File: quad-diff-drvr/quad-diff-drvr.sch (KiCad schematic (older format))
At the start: 58 parts, among them J1 Raspberry_Pi_2_3, J2 Conn_01x04, J3 Conn_01x04, J4 Conn_01x04, J5 Conn_01x04, J6 Conn_01x04, U1 INA3221, U2 74LS153, U3 74LS153, U4 74LS153, U5 PCA9555PW, U6 LTC1688, U7 SLG5NT1581V, U8 SLG5NT1581V

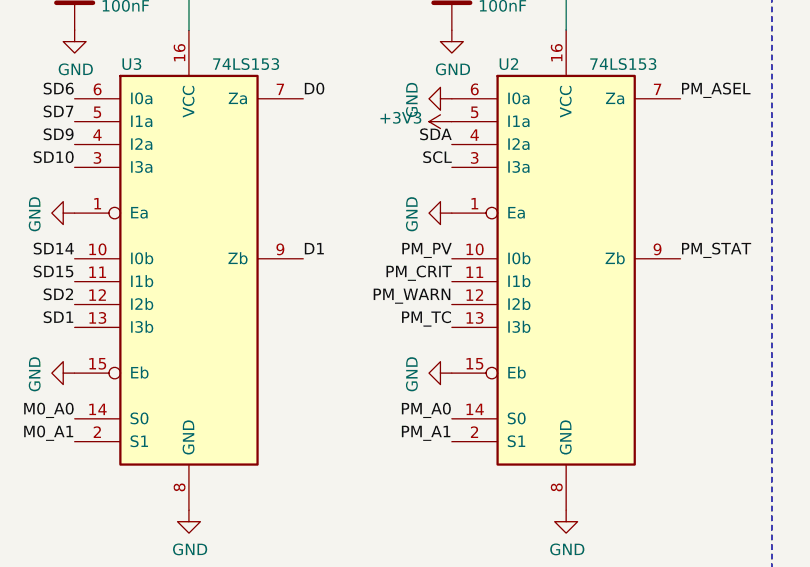
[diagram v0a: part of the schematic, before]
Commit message: qdd: two high-side switches in
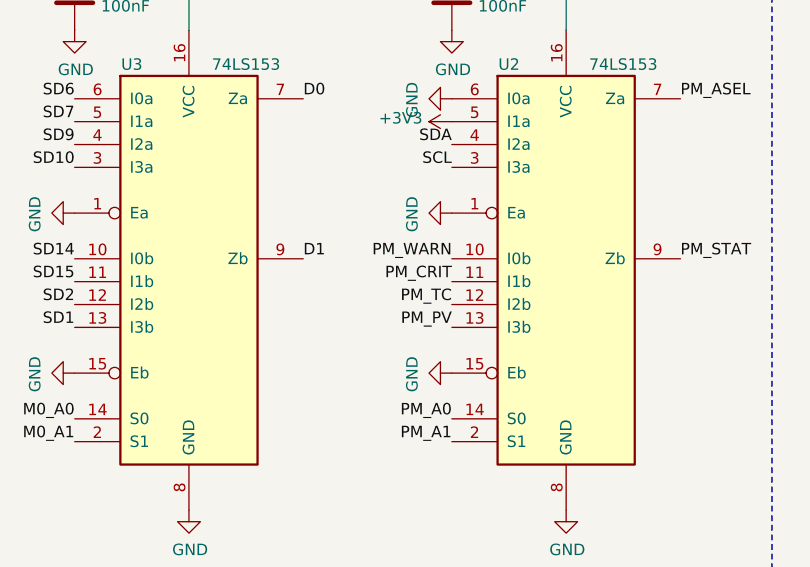
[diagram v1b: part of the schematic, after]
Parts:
- C14, C17: footprint Capacitor_SMD:C_0603_1608Metric -> Capacitor_SMD:C_1206_3216Metric
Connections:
- net PM_PV: now also U2.13 (I3b); no longer U2.10 (I0b)
- net PM_TC: now also U2.12 (I2b); no longer U2.13 (I3b)
- net PM_WARN: now also U2.10 (I0b); no longer U2.12 (I2b)
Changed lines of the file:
@@
 Text Label 5900 6000 2    50   ~ 0
 SCL
-Text Label 5900 6400 2    50   ~ 0
+Text Label 5900 6700 2    50   ~ 0
 PM_PV
 Text Label 5900 6500 2    50   ~ 0
 PM_CRIT
+Text Label 5900 6400 2    50   ~ 0
+PM_WARN
 Text Label 5900 6600 2    50   ~ 0
-PM_WARN
-Text Label 5900 6700 2    50   ~ 0
 PM_TC
 $Comp
@@
 F 0 "C14" H 8615 1246 50  0000 L CNN
 F 1 "10uF" H 8615 1155 50  0000 L CNN
-F 2 "Capacitor_SMD:C_0603_1608Metric" H 8538 1050 50  0001 C CNN
+F 2 "Capacitor_SMD:C_1206_3216Metric" H 8538 1050 50  0001 C CNN
 F 3 "~" H 8500 1200 50  0001 C CNN
 	1    8500 1200
@@
 F 0 "C17" H 10415 1246 50  0000 L CNN
 F 1 "10uF" H 10415 1155 50  0000 L CNN
-F 2 "Capacitor_SMD:C_0603_1608Metric" H 10338 1050 50  0001 C CNN
+F 2 "Capacitor_SMD:C_1206_3216Metric" H 10338 1050 50  0001 C CNN
 F 3 "~" H 10300 1200 50  0001 C CNN
 	1    10300 1200

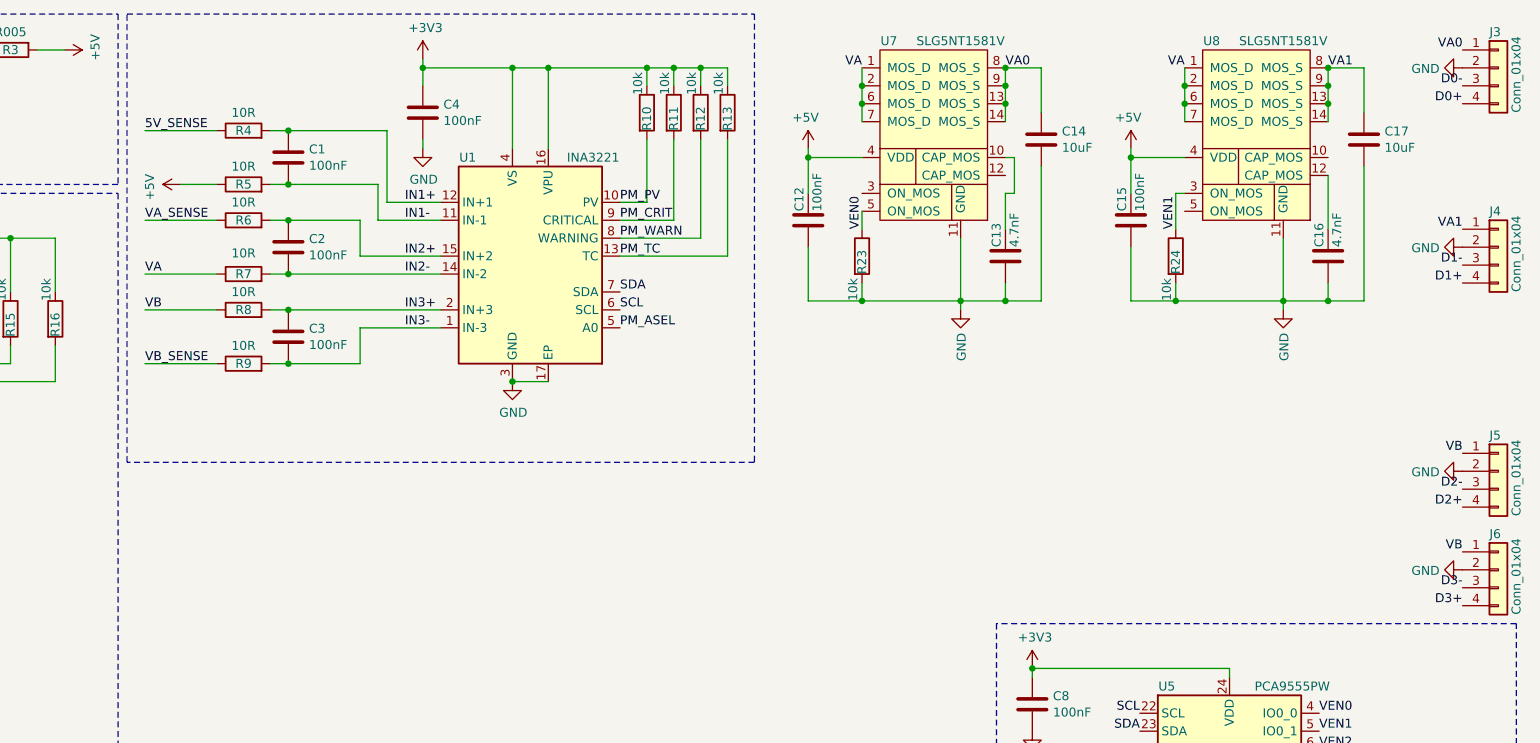
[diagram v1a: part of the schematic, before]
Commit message: qdd: VB high side switches
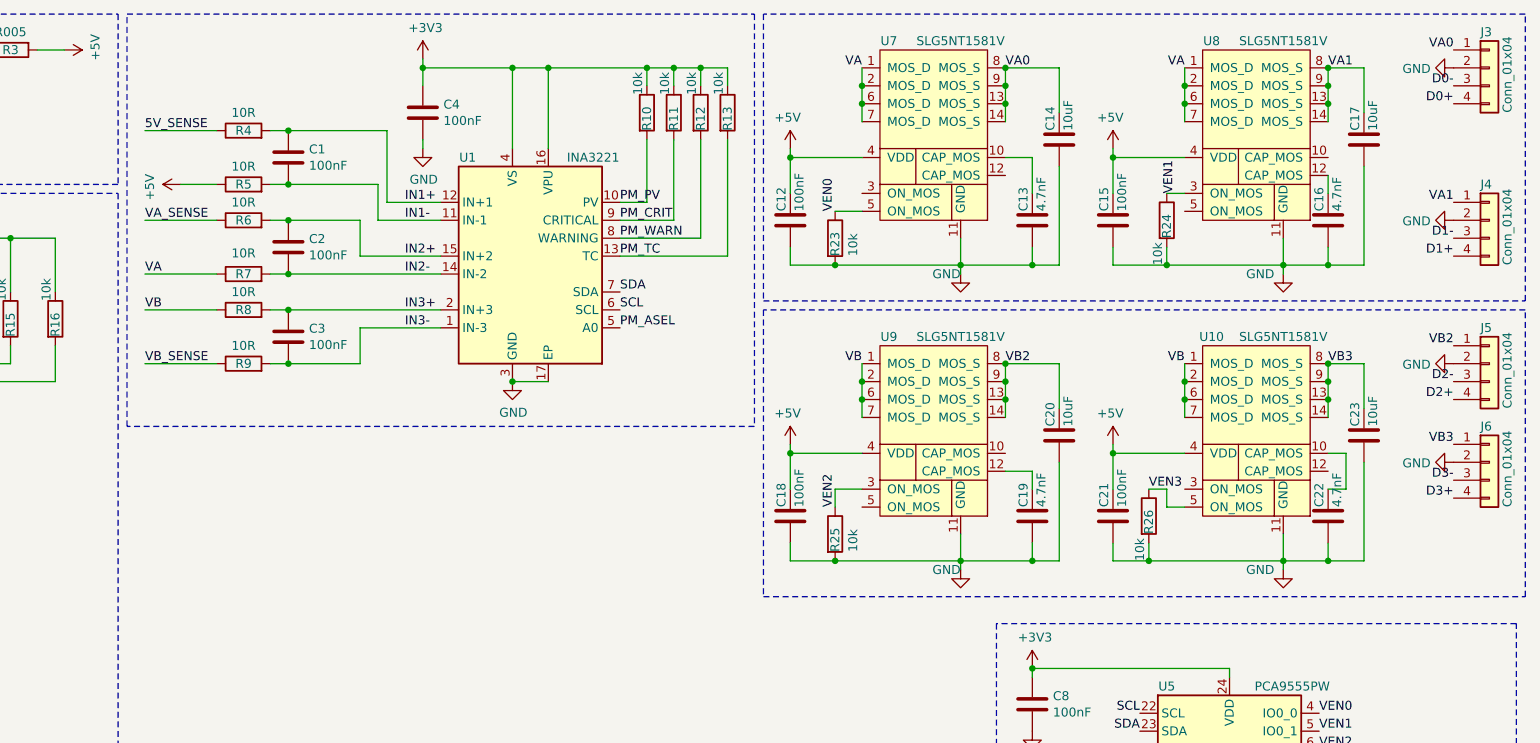
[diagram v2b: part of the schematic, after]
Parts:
- added C18, C21: 100nF, Capacitor_SMD:C_0603_1608Metric, symbol Device:C
- added C19, C22: 4.7nF, Capacitor_SMD:C_0603_1608Metric, symbol Device:C
- added C20, C23: 10uF, Capacitor_SMD:C_1206_3216Metric, symbol Device:C
- added R25, R26: 10k, Resistor_SMD:R_0603_1608Metric, symbol Device:R
- added U10, U9: SLG5NT1581V, octo-pcb:QFN-28_1x3_Pitch0.4mm, symbol octo-pcb:SLG5NT1581V
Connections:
- net +5V: now also C18.1, C21.1, U10.4 (VDD), U9.4 (VDD)
- net GND: now also C18.2, C19.2, C20.2, C21.2, C22.2, C23.2, R25.2, R26.2, U10.11 (GND), U9.11 (GND)
- net VB: now also U10.1 (MOS_D), U10.2 (MOS_D), U10.6 (MOS_D), U10.7 (MOS_D), U9.1 (MOS_D), U9.2 (MOS_D), U9.6 (MOS_D), U9.7 (MOS_D); no longer J5.1 (Pin_1), J6.1 (Pin_1)
- net VEN2: now also R25.1, U9.3 (ON_MOS)
- net VEN3: now also R26.1, U10.5 (ON_MOS)
- new net: C19.1, U9.12 (CAP_MOS)
- new net: C22.1, U10.10 (CAP_MOS)
- new net VB2: C20.1, J5.1 (Pin_1), U9.13 (MOS_S), U9.14 (MOS_S), U9.8 (MOS_S), U9.9 (MOS_S)
- new net VB3: C23.1, J6.1 (Pin_1), U10.13 (MOS_S), U10.14 (MOS_S), U10.8 (MOS_S), U10.9 (MOS_S)
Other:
- moved on the sheet: C12, C13, C14, C15, C16, J3, J4, J5, J6, R23, R24

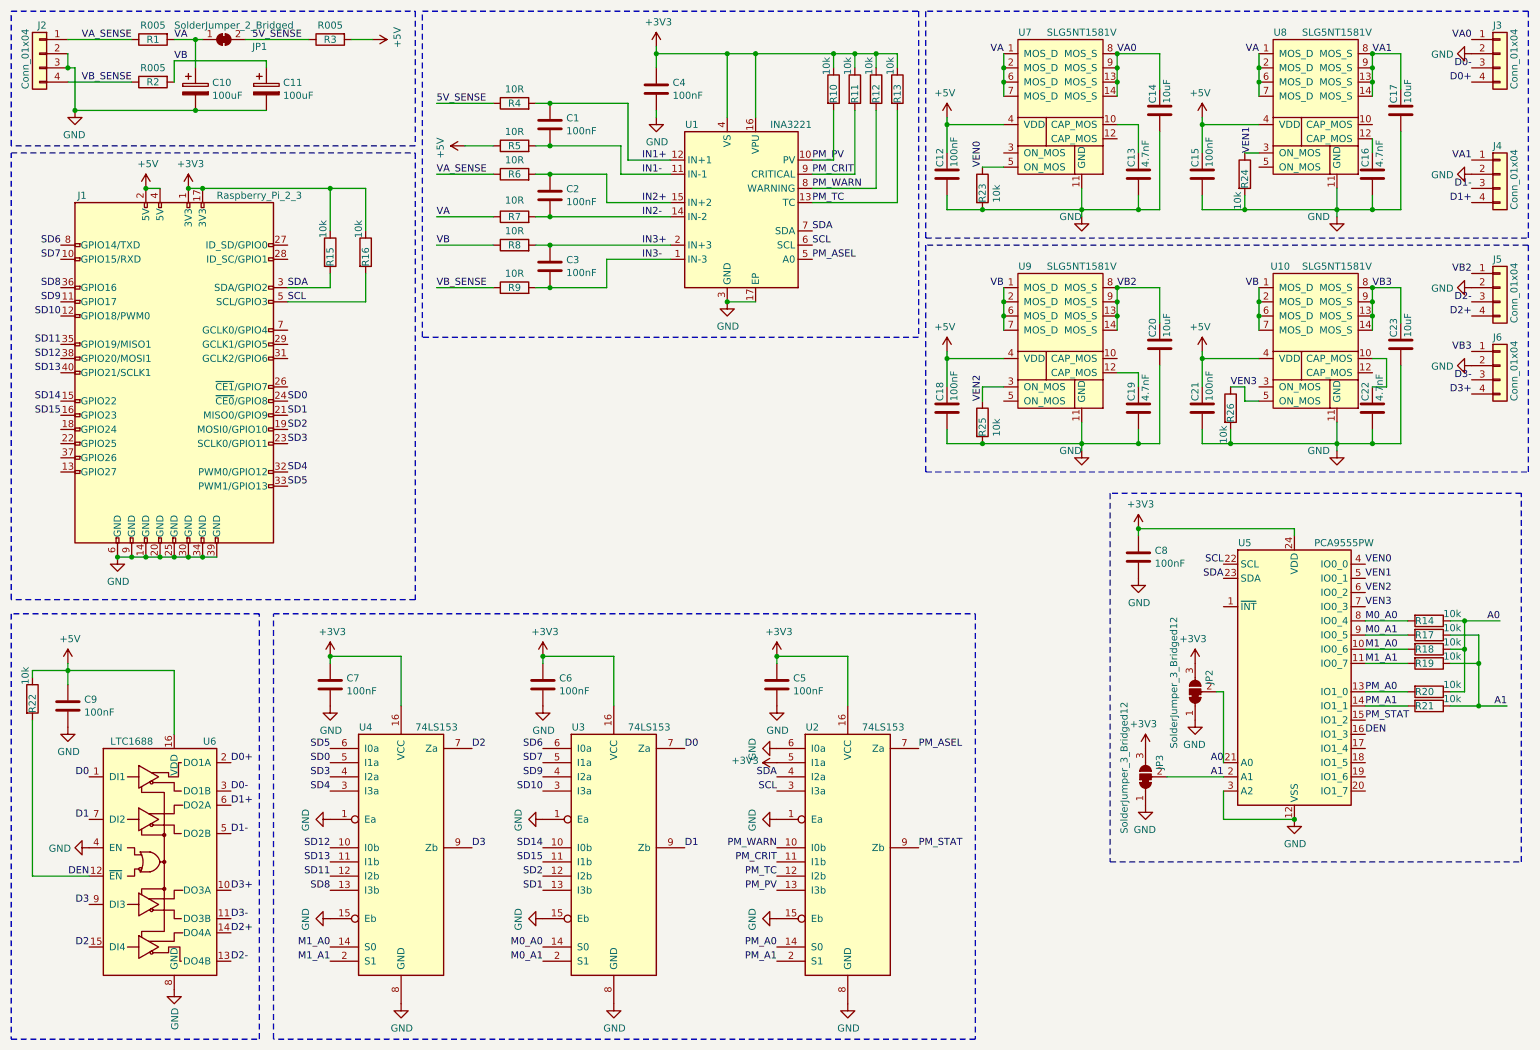
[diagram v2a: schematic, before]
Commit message: qdd: quick and dirty route done
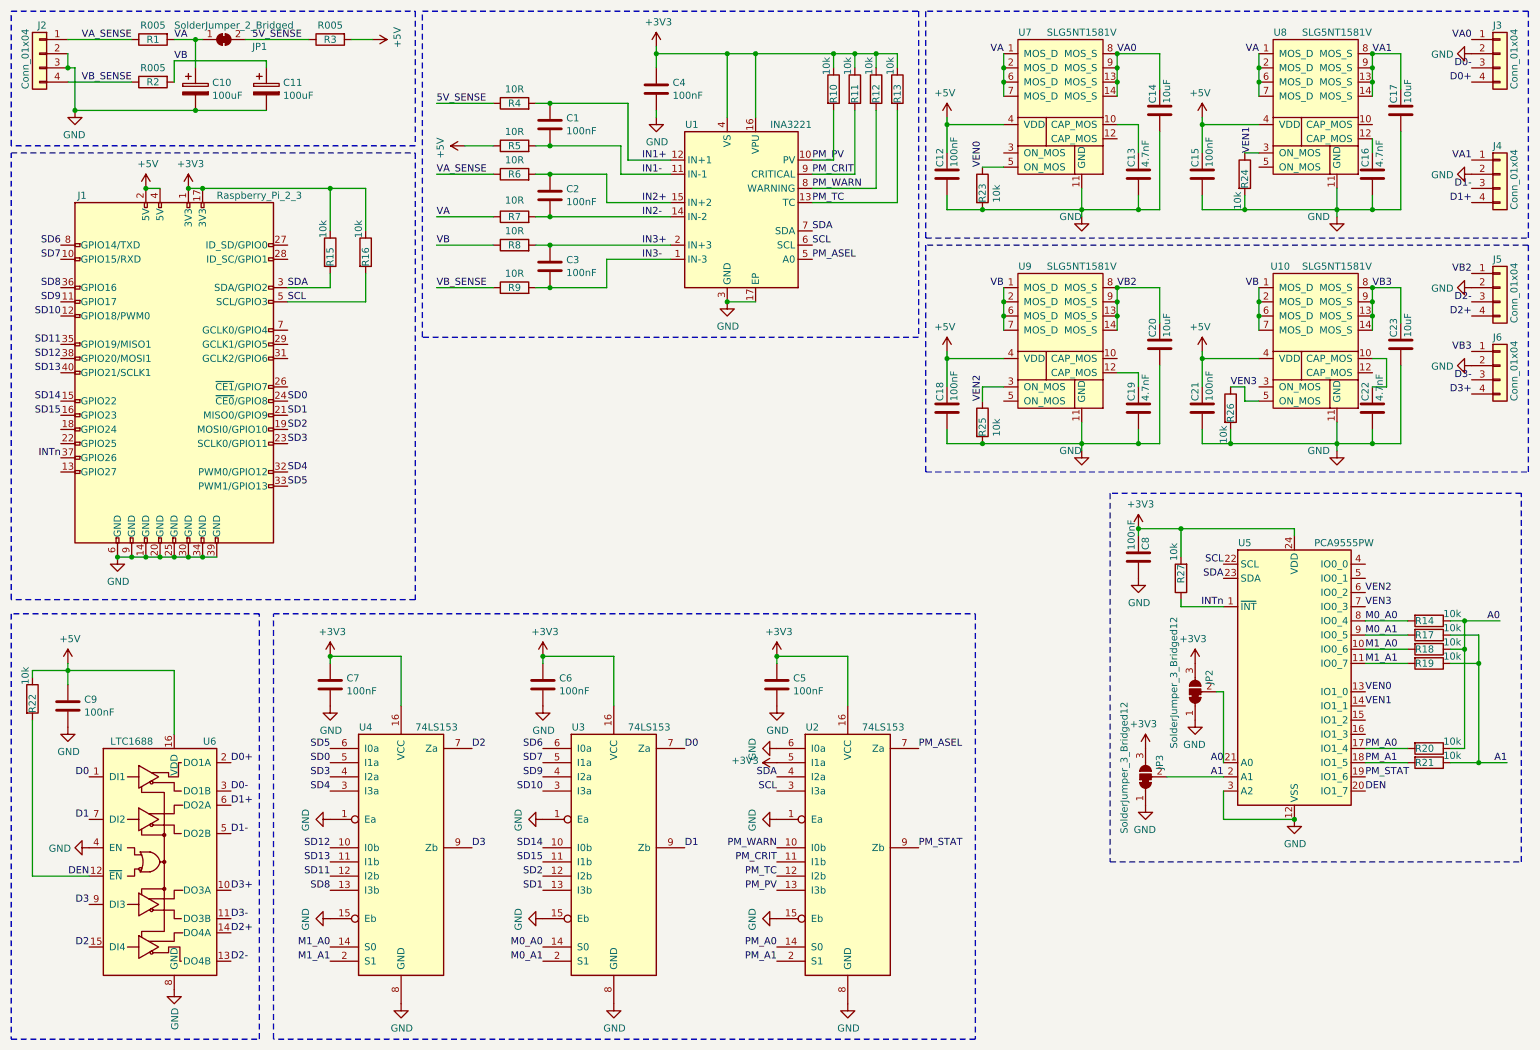
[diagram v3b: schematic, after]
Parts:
- added R27: 10k, Resistor_SMD:R_0603_1608Metric, symbol Device:R
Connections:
- net +3V3: now also R27.2
- net DEN: now also U5.20 (IO1_7); no longer U5.16 (IO1_3)
- net PM_A0: now also U5.17 (IO1_4); no longer U5.13 (IO1_0)
- net PM_A1: now also U5.18 (IO1_5); no longer U5.14 (IO1_1)
- net PM_STAT: now also U5.19 (IO1_6); no longer U5.15 (IO1_2)
- net VEN0: now also U5.13 (IO1_0); no longer U5.4 (IO0_0)
- net VEN1: now also U5.14 (IO1_1); no longer U5.5 (IO0_1)
- net INTn: now reaches J1.37 (GPIO26)
- net INTn: now also U5.1 (~INT), R27.1
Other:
- moved on the sheet: R20, R21
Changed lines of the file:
@@
 	6400 5050 6400 5400
 Connection ~ 5900 5050
-Text Label 10050 5300 0    50   ~ 0
+Text Label 10050 5700 0    50   ~ 0
 PM_A0
 Text Label 5900 7100 2    50   ~ 0
@@
 Text Label 9050 5900 2    50   ~ 0
 A1
-Text Label 10050 4400 0    50   ~ 0
+Text Label 10050 5300 0    50   ~ 0
 VEN0
-Text Label 10050 4500 0    50   ~ 0
+Text Label 10050 5400 0    50   ~ 0
 VEN1
 Text Label 10050 4600 0    50   ~ 0
@@
 Text Label 6900 5700 0    50   ~ 0
 PM_ASEL
-Text Label 10050 5400 0    50   ~ 0
+Text Label 10050 5800 0    50   ~ 0
 PM_A1
-Text Label 10050 5500 0    50   ~ 0
+Text Label 10050 5900 0    50   ~ 0
 PM_STAT
 $Comp
@@
 U 1 1 621687EB
 P 8450 4350
-F 0 "C8" H 8565 4396 50  0000 L CNN
-F 1 "100nF" H 8565 4305 50  0000 L CNN
+F 0 "C8" V 8500 4400 50  0000 L CNN
+F 1 "100nF" V 8400 4400 50  0000 L CNN
 F 2 "Capacitor_SMD:C_0603_1608Metric" H 8488 4200 50  0001 C CNN
 F 3 "~" H 8450 4350 50  0001 C CNN
@@
 	8450 4150 8450 4200
 Wire Wire Line
-	8450 4150 9550 4150
+	8450 4150 8750 4150
 Connection ~ 8450 4150
 $Comp
@@
 L Device:R R20
 U 1 1 6221731B
-P 10500 5300
-F 0 "R20" V 10500 5200 50  0000 L CNN
-F 1 "10k" V 10450 5400 50  0000 L CNN
-F 2 "Resistor_SMD:R_0603_1608Metric" V 10430 5300 50  0001 C CNN
-F 3 "~" H 10500 5300 50  0001 C CNN
-	1    10500 5300
+P 10500 5700
+F 0 "R20" V 10500 5600 50  0000 L CNN
+F 1 "10k" V 10450 5800 50  0000 L CNN
+F 2 "Resistor_SMD:R_0603_1608Metric" V 10430 5700 50  0001 C CNN
+F 3 "~" H 10500 5700 50  0001 C CNN
+	1    10500 5700
 	0    1    1    0
 $EndComp
@@
 L Device:R R21
 U 1 1 6221779B
-P 10500 5400
-F 0 "R21" V 10500 5300 50  0000 L CNN
-F 1 "10k" V 10450 5500 50  0000 L CNN
-F 2 "Resistor_SMD:R_0603_1608Metric" V 10430 5400 50  0001 C CNN
-F 3 "~" H 10500 5400 50  0001 C CNN
-	1    10500 5400
+P 10500 5800
+F 0 "R21" V 10500 5700 50  0000 L CNN
+F 1 "10k" V 10450 5900 50  0000 L CNN
+F 2 "Resistor_SMD:R_0603_1608Metric" V 10430 5800 50  0001 C CNN
+F 3 "~" H 10500 5800 50  0001 C CNN
+	1    10500 5800
 	0    1    1    0
 $EndComp
@@
 	10750 4800 10750 5000
 Wire Wire Line
-	10750 5300 10650 5300
+	10750 5700 10650 5700
 Wire Wire Line
 	10650 5000 10750 5000
 Connection ~ 10750 5000
 Wire Wire Line
-	10750 5000 10750 5300
+	10750 5000 10750 5700
 Wire Wire Line
 	10650 4900 10850 4900
@@
 	10850 4900 10850 5100
 Wire Wire Line
-	10850 5400 10650 5400
+	10850 5800 10650 5800
 Wire Wire Line
 	10650 5100 10850 5100
 Connection ~ 10850 5100
 Wire Wire Line
-	10850 5100 10850 5400
+	10850 5100 10850 5800
 Wire Wire Line
 	10350 4800 10050 4800
@@
 Wire Wire Line
 	10350 5100 10050 5100
-Wire Wire Line
-	10350 5300 10050 5300
-Wire Wire Line
-	10350 5400 10050 5400
 Wire Wire Line
 	11000 4800 10750 4800
@@
 A0
 Wire Wire Line
-	11050 5400 10850 5400
-Connection ~ 10850 5400
-Text Label 11050 5400 2    50   ~ 0
+	11050 5800 10850 5800
+Connection ~ 10850 5800
+Text Label 11050 5800 2    50   ~ 0
 A1
 $Comp
@@
 	1    0    0    -1
 $EndComp
-Text Label 10050 5600 0    50   ~ 0
+Text Label 10050 6000 0    50   ~ 0
 DEN
 Text Label 1050 6600 2    50   ~ 0
@@
 Wire Wire Line
 	10200 2950 10100 2950
+Text Label 9050 4700 2    50   ~ 0
+INTn
+$Comp
+L Device:R R27
+U 1 1 6231E652
+P 8750 4500
+F 0 "R27" V 8750 4400 50  0000 L CNN
+F 1 "10k" V 8800 4250 50  0000 L CNN
+F 2 "Resistor_SMD:R_0603_1608Metric" V 8680 4500 50  0001 C CNN
+F 3 "~" H 8750 4500 50  0001 C CNN
+	1    8750 4500
+	-1   0    0    1
+$EndComp
+Wire Wire Line
+	9050 4700 8750 4700
+Wire Wire Line
+	8750 4700 8750 4650
+Wire Wire Line
+	8750 4350 8750 4150
+Connection ~ 8750 4150
+Wire Wire Line
+	8750 4150 9550 4150
+Text Label 850  3650 2    50   ~ 0
+INTn
+Wire Wire Line
+	10350 5700 10050 5700
+Wire Wire Line
+	10350 5800 10050 5800
 $EndSCHEMATC
